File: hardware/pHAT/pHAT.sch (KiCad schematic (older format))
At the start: 5 parts, among them P1 Conn_02x20_Odd_Even

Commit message: First version of PCB for pHAT
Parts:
- added C0: 0.1µ, Capacitor_SMD:C_0805_2012Metric_Pad1.15x1.40mm_HandSolder, symbol Device:C
- added C1: 4.7µ, Capacitor_SMD:C_0805_2012Metric_Pad1.15x1.40mm_HandSolder, symbol Device:C
- added J_Air1, J_Hive1: Conn_01x04, Connector_Molex:Molex_KK-254_AE-6410-04A_1x04_P2.54mm_Vertical, symbol Connector_Generic:Conn_01x04
- added J_Weight1: Conn_01x02, Connector_Molex:Molex_KK-254_AE-6410-02A_1x02_P2.54mm_Vertical, symbol Connector_Generic:Conn_01x02
- added R0, R1, R2, R3, R4, R5, R6, R7, R8: 5K, Resistor_SMD:R_0805_2012Metric_Pad1.15x1.40mm_HandSolder, symbol Device:R
- added U0: PCA9540B, Package_SO:TSSOP-8_3x3mm_P0.65mm, symbol Interface_Expansion:PCA9540B
- added U1: ADC101C021CIMK, Package_TO_SOT_SMD:SOT-23-6, symbol Analog_ADC:ADC101C021CIMK
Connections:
- net labels added: +3V3, AnalogIn, SCL0, SCL1, SDA0, SDA1
- wire segments 22 -> 49

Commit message: Moving form multiplexer to two I2C busses
Changed from using one I2C bus with a multiplexer to using two I2C busses with the addition of level shifters
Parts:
- removed U0: PCA9540B, Package_SO:TSSOP-8_3x3mm_P0.65mm, symbol Interface_Expansion:PCA9540B
- added R10, R9: 5K, Resistor_SMD:R_0805_2012Metric_Pad1.15x1.40mm_HandSolder, symbol Device:R
- added U2, U3: P82B96, Package_SO:SOIC-8_3.9x4.9mm_P1.27mm, symbol Interface_Expansion:P82B96
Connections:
- net labels added: ADC_Alert, SCLA, SCLH, SDAA, SDAH
- net labels removed: SCL, SDA
- wire segments 49 -> 63
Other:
- moved on the sheet: J_Air1, J_Hive1, J_Weight1, R3, R4, R5, R6, R7, R8

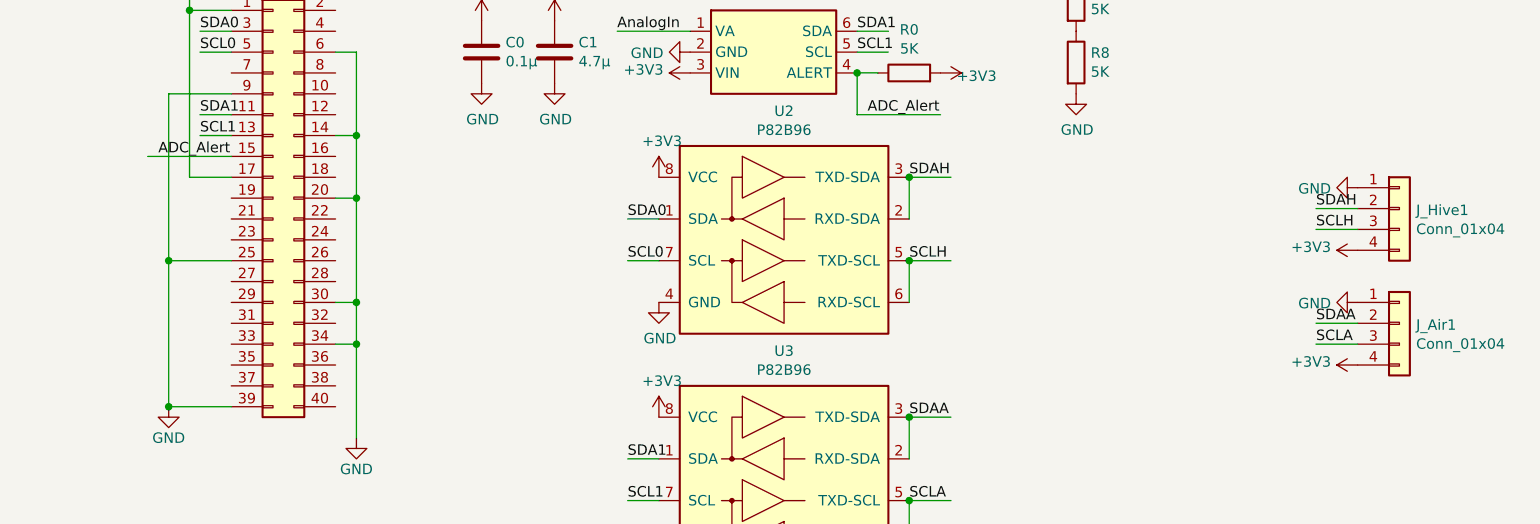
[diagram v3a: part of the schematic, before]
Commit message: Added the alarm pin for humidity
Added support for the alarm pin of the HIH6131 in order to detect through interrupt a high level of humidity
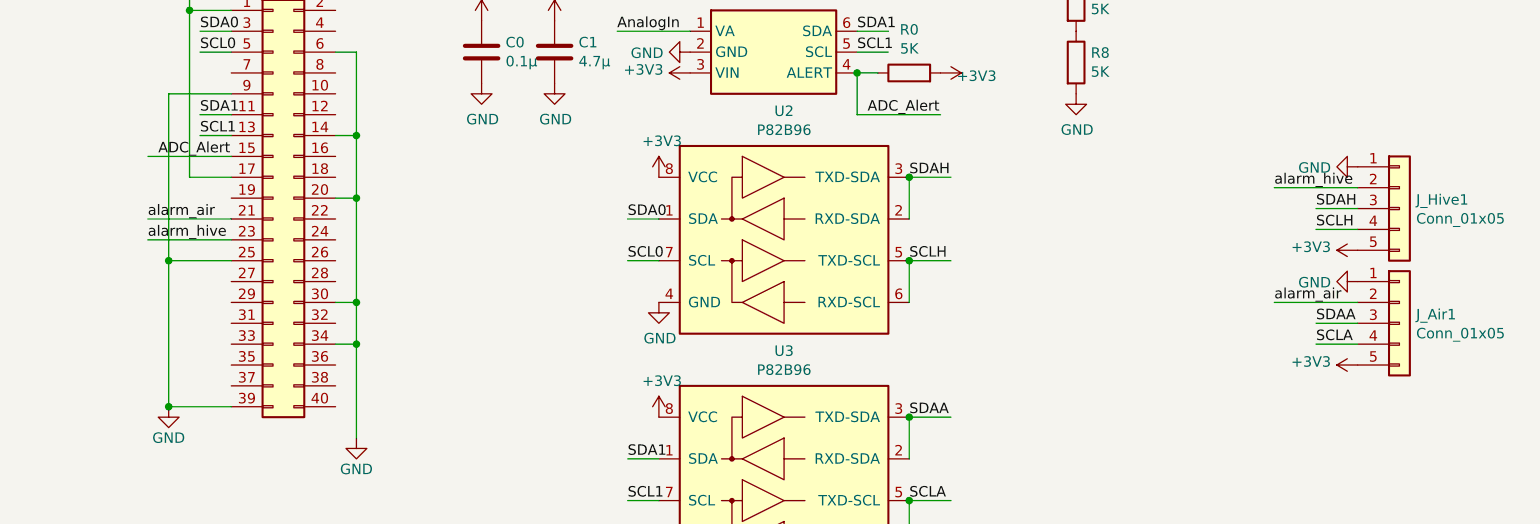
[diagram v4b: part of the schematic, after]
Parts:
- removed J_Air1, J_Hive1: Conn_01x04, Connector_Molex:Molex_KK-254_AE-6410-04A_1x04_P2.54mm_Vertical, symbol Connector_Generic:Conn_01x04
- added J_Air1, J_Hive1: Conn_01x05, Connector_Molex:Molex_KK-254_AE-6410-05A_1x05_P2.54mm_Vertical, symbol Connector_Generic:Conn_01x05
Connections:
- net labels added: alarm_air, alarm_hive
- wire segments 63 -> 67
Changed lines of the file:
@@
 Sheet 1 1
 Title "Beehive pHAT"
-Date "2019-01-21"
-Rev "v2.0"
+Date "2019-01-29"
+Rev "v2.1"
 Comp "University of Glasgow"
 Comment1 ""
@@
 $EndComp
 $Comp
-L Connector_Generic:Conn_01x04 J_Air1
-U 1 1 5C4706C5
-P 8000 2600
-F 0 "J_Air1" H 8080 2592 50  0000 L CNN
-F 1 "Conn_01x04" H 8080 2501 50  0000 L CNN
-F 2 "Connector_Molex:Molex_KK-254_AE-6410-04A_1x04_P2.54mm_Vertical" H 8000 2600 50  0001 C CNN
-F 3 "~" H 8000 2600 50  0001 C CNN
-	1    8000 2600
-	1    0    0    -1
-$EndComp
-$Comp
-L Connector_Generic:Conn_01x04 J_Hive1
-U 1 1 5C470742
-P 8000 2050
-F 0 "J_Hive1" H 8080 2042 50  0000 L CNN
-F 1 "Conn_01x04" H 8080 1951 50  0000 L CNN
-F 2 "Connector_Molex:Molex_KK-254_AE-6410-04A_1x04_P2.54mm_Vertical" H 8000 2050 50  0001 C CNN
-F 3 "~" H 8000 2050 50  0001 C CNN
-	1    8000 2050
-	1    0    0    -1
-$EndComp
-$Comp
 L Connector_Generic:Conn_01x02 J_Weight1
 U 1 1 5C4707D9
@@
 L power:GND #PWR0120
 U 1 1 5C47784F
-P 7800 1950
-F 0 "#PWR0120" H 7800 1700 50  0001 C CNN
-F 1 "GND" V 7805 1822 50  0000 R CNN
-F 2 "" H 7800 1950 50  0001 C CNN
-F 3 "" H 7800 1950 50  0001 C CNN
-	1    7800 1950
+P 7800 1850
+F 0 "#PWR0120" H 7800 1600 50  0001 C CNN
+F 1 "GND" V 7805 1722 50  0000 R CNN
+F 2 "" H 7800 1850 50  0001 C CNN
+F 3 "" H 7800 1850 50  0001 C CNN
+	1    7800 1850
 	0    1    1    0
 $EndComp
@@
 L power:GND #PWR0121
 U 1 1 5C4780F6
-P 7800 2500
-F 0 "#PWR0121" H 7800 2250 50  0001 C CNN
-F 1 "GND" V 7805 2372 50  0000 R CNN
-F 2 "" H 7800 2500 50  0001 C CNN
-F 3 "" H 7800 2500 50  0001 C CNN
-	1    7800 2500
+P 7800 2400
+F 0 "#PWR0121" H 7800 2150 50  0001 C CNN
+F 1 "GND" V 7805 2272 50  0000 R CNN
+F 2 "" H 7800 2400 50  0001 C CNN
+F 3 "" H 7800 2400 50  0001 C CNN
+	1    7800 2400
 	0    1    1    0
 $EndComp
@@
 Text Label 2050 1800 0    50   ~ 0
 ADC_Alert
+$Comp
+L Connector_Generic:Conn_01x05 J_Hive1
+U 1 1 5C50B69B
+P 8000 2050
+F 0 "J_Hive1" H 8080 2092 50  0000 L CNN
+F 1 "Conn_01x05" H 8080 2001 50  0000 L CNN
+F 2 "Connector_Molex:Molex_KK-254_AE-6410-05A_1x05_P2.54mm_Vertical" H 8000 2050 50  0001 C CNN
+F 3 "~" H 8000 2050 50  0001 C CNN
+	1    8000 2050
+	1    0    0    -1
+$EndComp
+$Comp
+L Connector_Generic:Conn_01x05 J_Air1
+U 1 1 5C50B707
+P 8000 2600
+F 0 "J_Air1" H 8080 2642 50  0000 L CNN
+F 1 "Conn_01x05" H 8080 2551 50  0000 L CNN
+F 2 "Connector_Molex:Molex_KK-254_AE-6410-05A_1x05_P2.54mm_Vertical" H 8000 2600 50  0001 C CNN
+F 3 "~" H 8000 2600 50  0001 C CNN
+	1    8000 2600
+	1    0    0    -1
+$EndComp
+Text Label 7400 2500 0    50   ~ 0
+alarm_air
+Text Label 7400 1950 0    50   ~ 0
+alarm_hive
+Wire Wire Line
+	7800 2500 7400 2500
+Wire Wire Line
+	7800 1950 7400 1950
+Text Label 2000 2200 0    50   ~ 0
+alarm_hive
+Wire Wire Line
+	2400 2200 2000 2200
+Text Label 2000 2100 0    50   ~ 0
+alarm_air
+Wire Wire Line
+	2400 2100 2000 2100
 $EndSCHEMATC

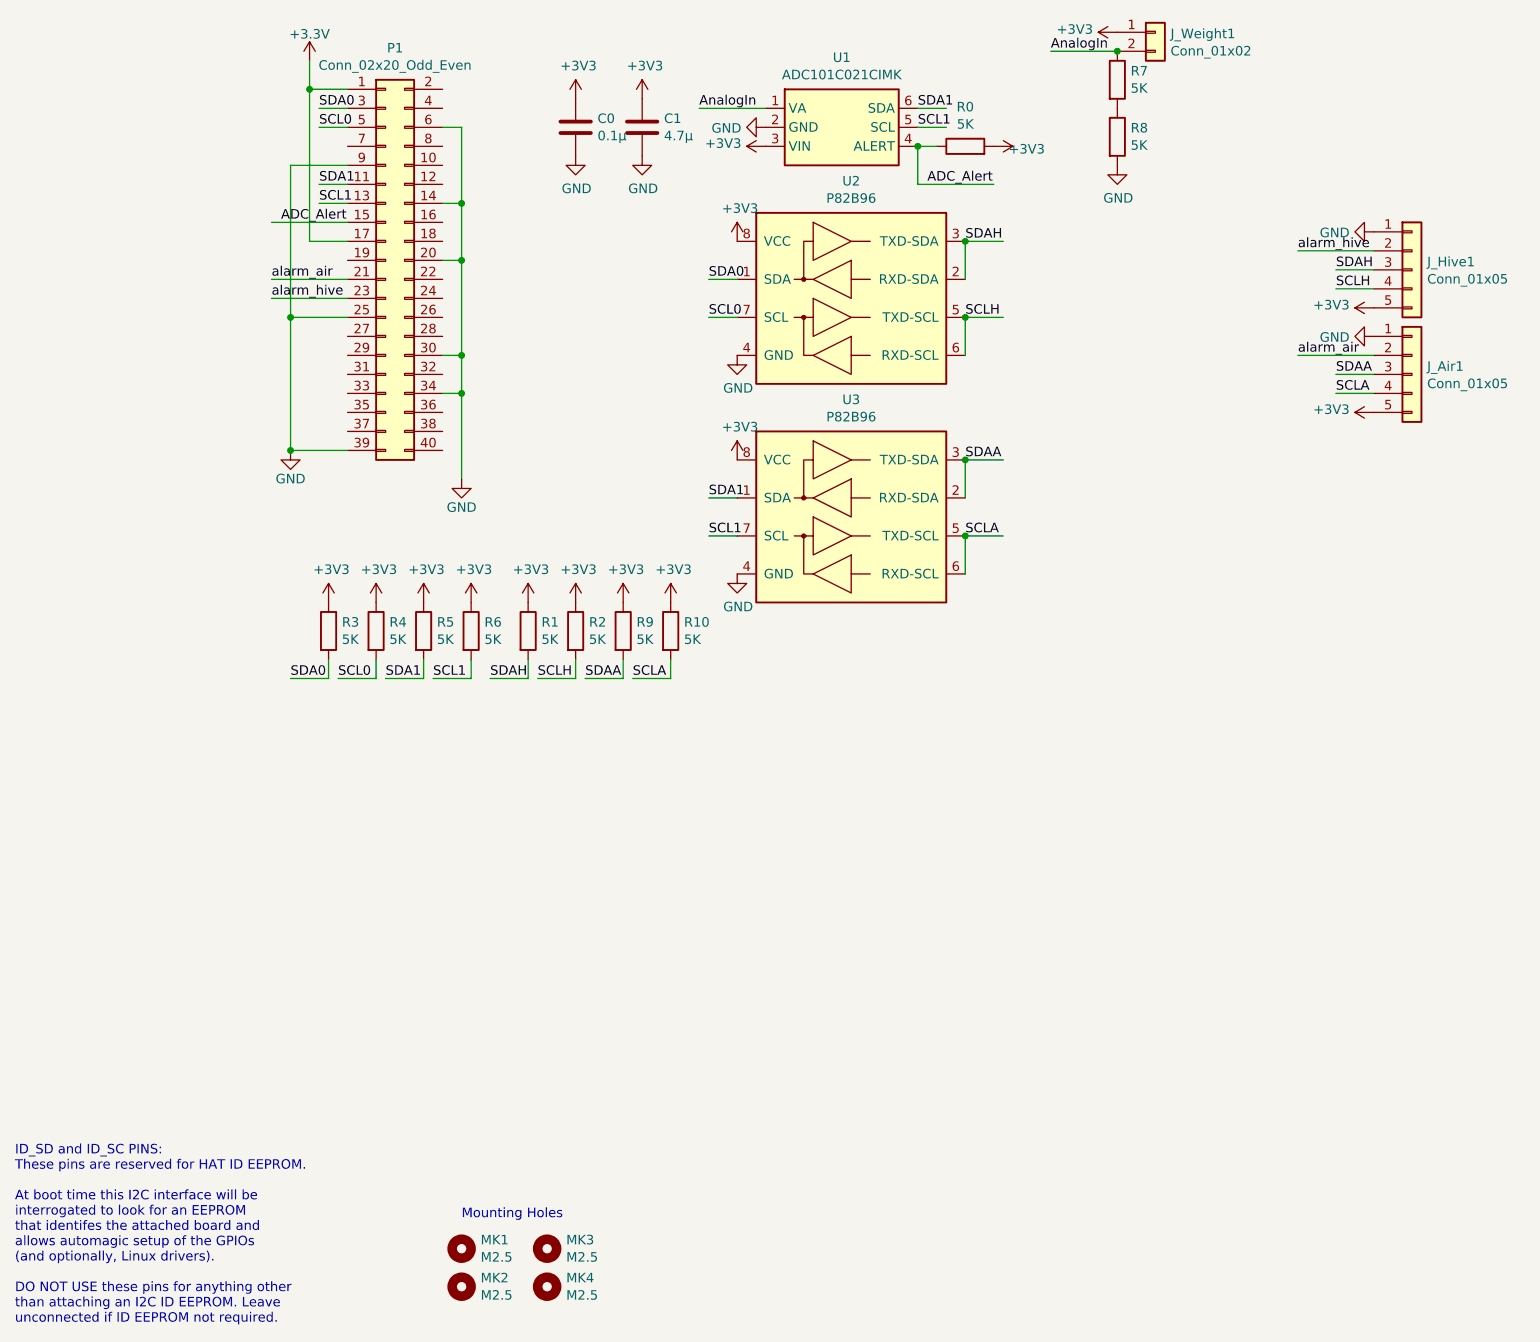
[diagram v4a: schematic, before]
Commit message: Sensor Board v3.0
Removed ADC converter, moved the hive temp&hum sensor to the main board that will now be placed inside the hive
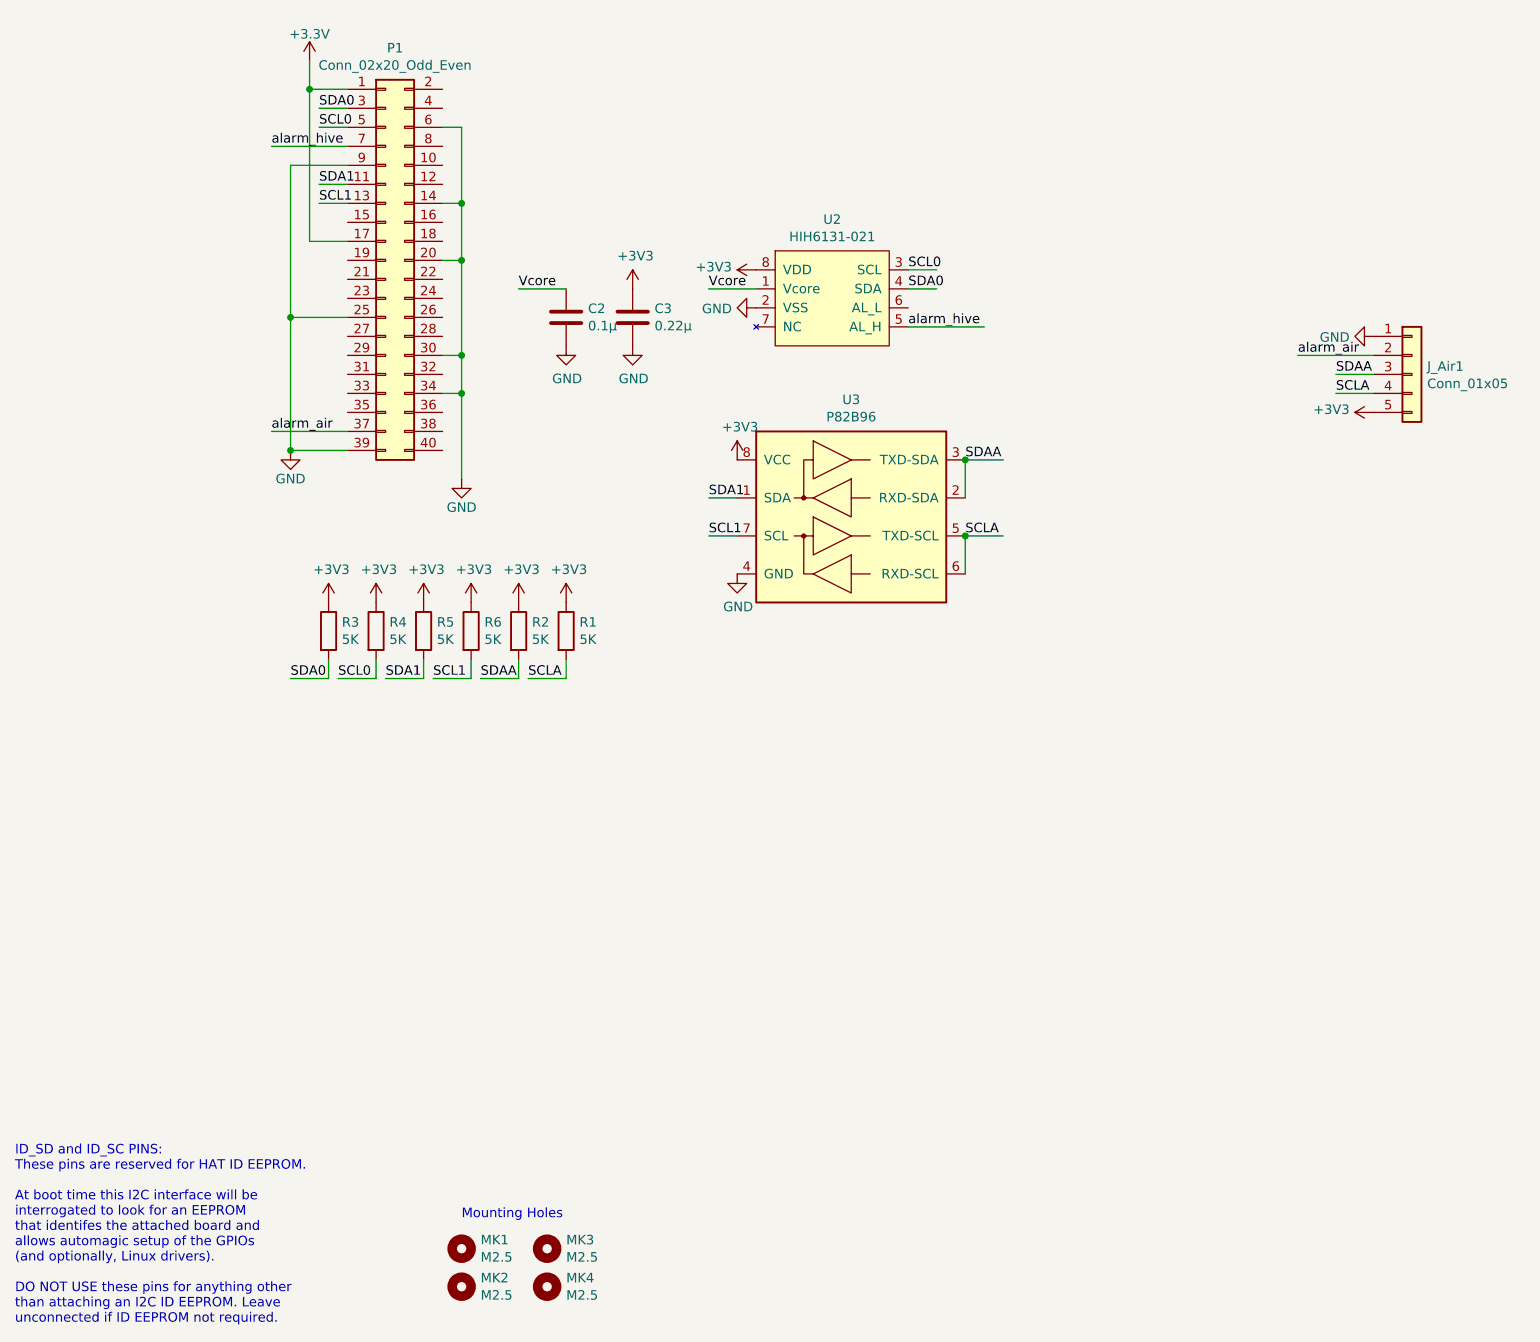
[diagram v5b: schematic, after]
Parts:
- removed C0: 0.1µ, Capacitor_SMD:C_0805_2012Metric_Pad1.15x1.40mm_HandSolder, symbol Device:C
- removed C1: 4.7µ, Capacitor_SMD:C_0805_2012Metric_Pad1.15x1.40mm_HandSolder, symbol Device:C
- removed J_Hive1: Conn_01x05, Connector_Molex:Molex_KK-254_AE-6410-05A_1x05_P2.54mm_Vertical, symbol Connector_Generic:Conn_01x05
- removed J_Weight1: Conn_01x02, Connector_Molex:Molex_KK-254_AE-6410-02A_1x02_P2.54mm_Vertical, symbol Connector_Generic:Conn_01x02
- removed R0, R1, R2, R7, R8: 5K, Resistor_SMD:R_0805_2012Metric_Pad1.15x1.40mm_HandSolder, symbol Device:R
- removed U1: ADC101C021CIMK, Package_TO_SOT_SMD:SOT-23-6, symbol Analog_ADC:ADC101C021CIMK
- removed U2: P82B96, Package_SO:SOIC-8_3.9x4.9mm_P1.27mm, symbol Interface_Expansion:P82B96
- added C2: 0.1µ, Capacitor_SMD:C_0805_2012Metric_Pad1.15x1.40mm_HandSolder, symbol Device:C
- added C3: 0.22µ, Capacitor_SMD:C_0805_2012Metric_Pad1.15x1.40mm_HandSolder, symbol Device:C
- added U2: HIH6131-021, Package_SO:SOIC-8_3.9x4.9mm_P1.27mm, symbol honeywell:HIHxx3x-021
- renumbered R10 to R1, R9 to R2
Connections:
- net labels added: Vcore
- net labels removed: ADC_Alert, AnalogIn, SCLH, SDAH
- wire segments 67 -> 51
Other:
- moved on the sheet: R1, R2
